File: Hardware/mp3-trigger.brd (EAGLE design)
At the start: 58.4 x 62.2 mm, 90 parts, among them J1 POWER_JACKTOE, Q1 12.288MHz, U1 CY8C29466, U10 M18_, U2 USD-SOCKET, U3 MUX-74HC4067SMD, U4 LM1117, U5 1.8V Reg, U6 NAV_SWITCHSMD, U7 VS1063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

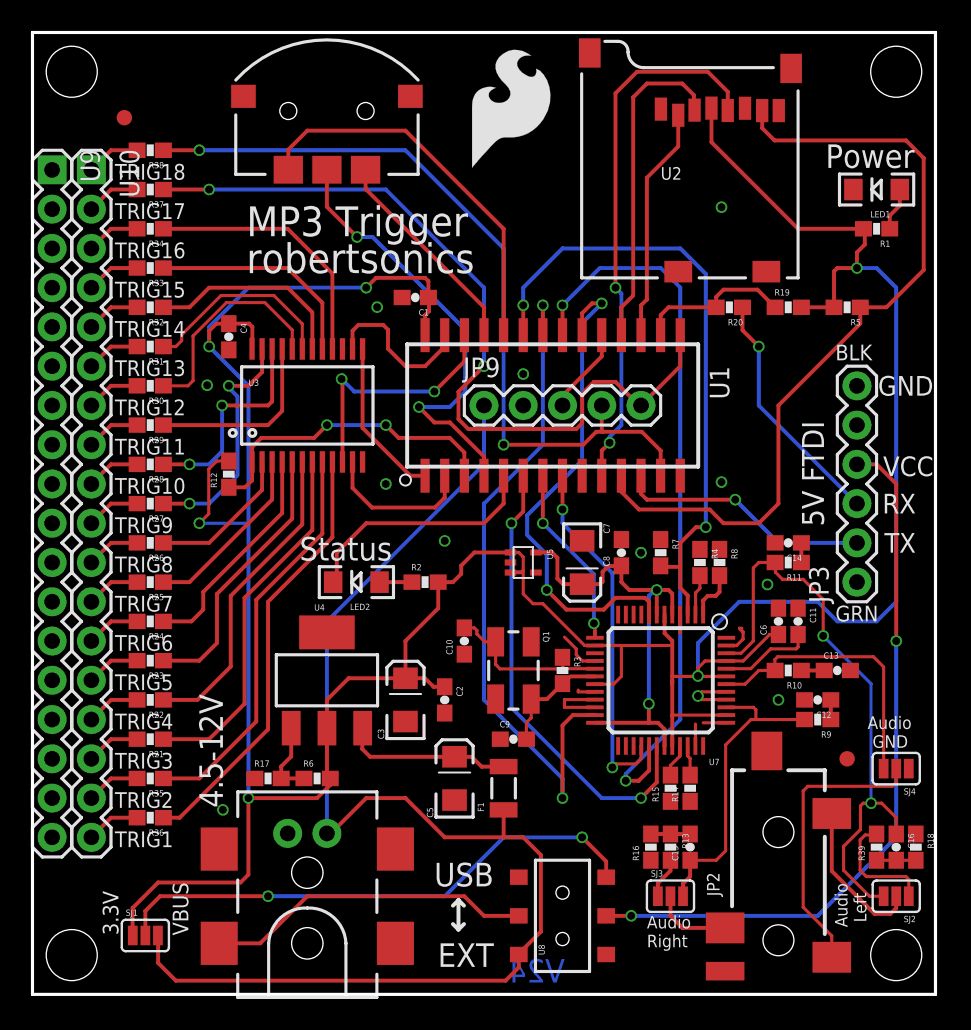
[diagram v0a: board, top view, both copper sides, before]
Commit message: V24 Reds Checklist Updates
See github for issues fixed
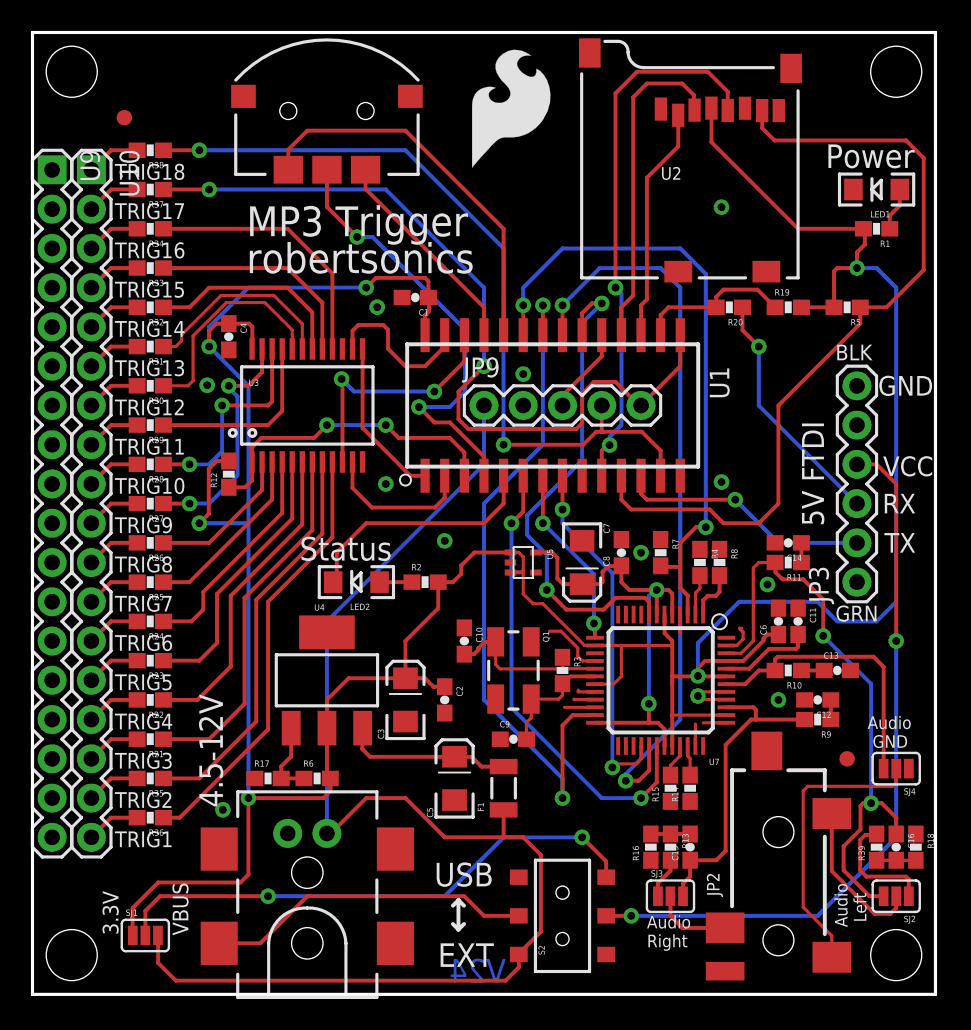
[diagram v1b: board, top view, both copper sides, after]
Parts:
- turned C10 to 270 degrees
- renumbered U6 to S1, U8 to S2
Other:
- board text added: "Headphone out (DC)"
- board text added: "Line out (AC - default)"
- board text removed: "Headphone out"
- board text removed: "Line out (default)"
